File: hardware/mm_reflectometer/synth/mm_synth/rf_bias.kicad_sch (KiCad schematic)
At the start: 28 parts

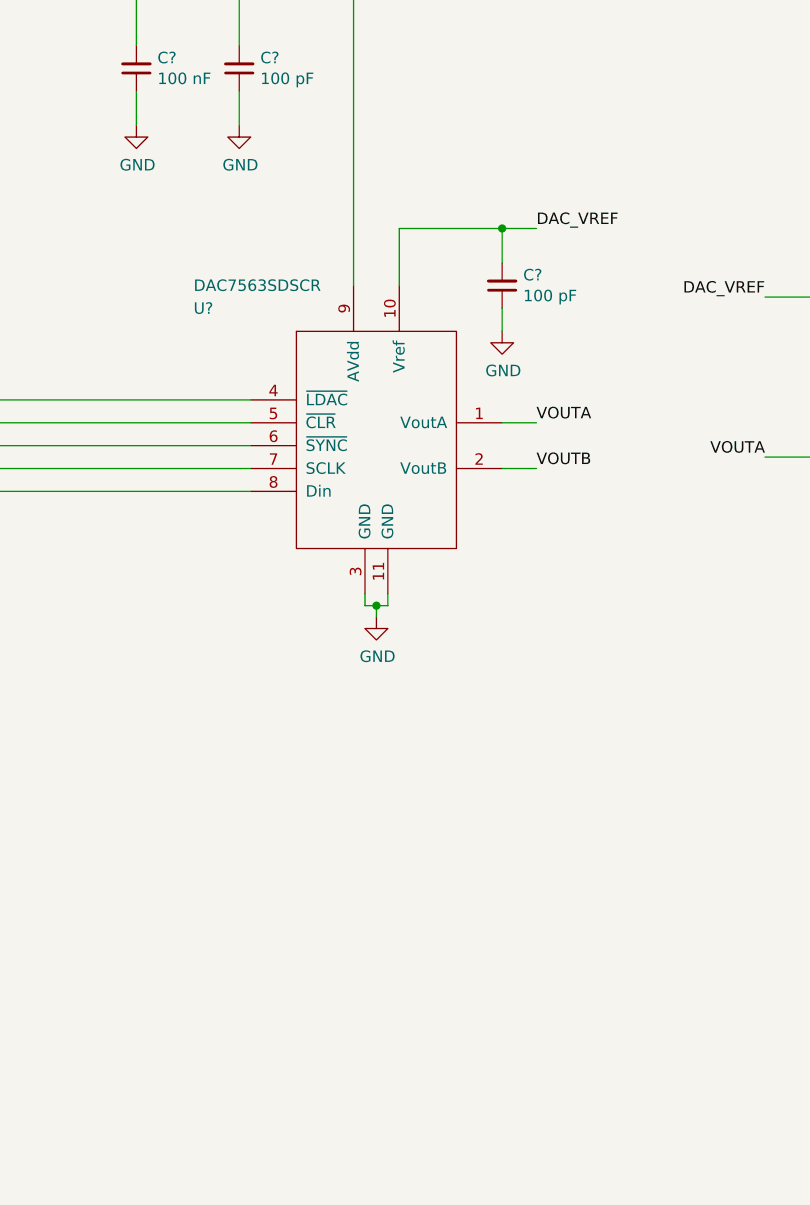
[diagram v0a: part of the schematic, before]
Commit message: adding bias circuitry to mm synth
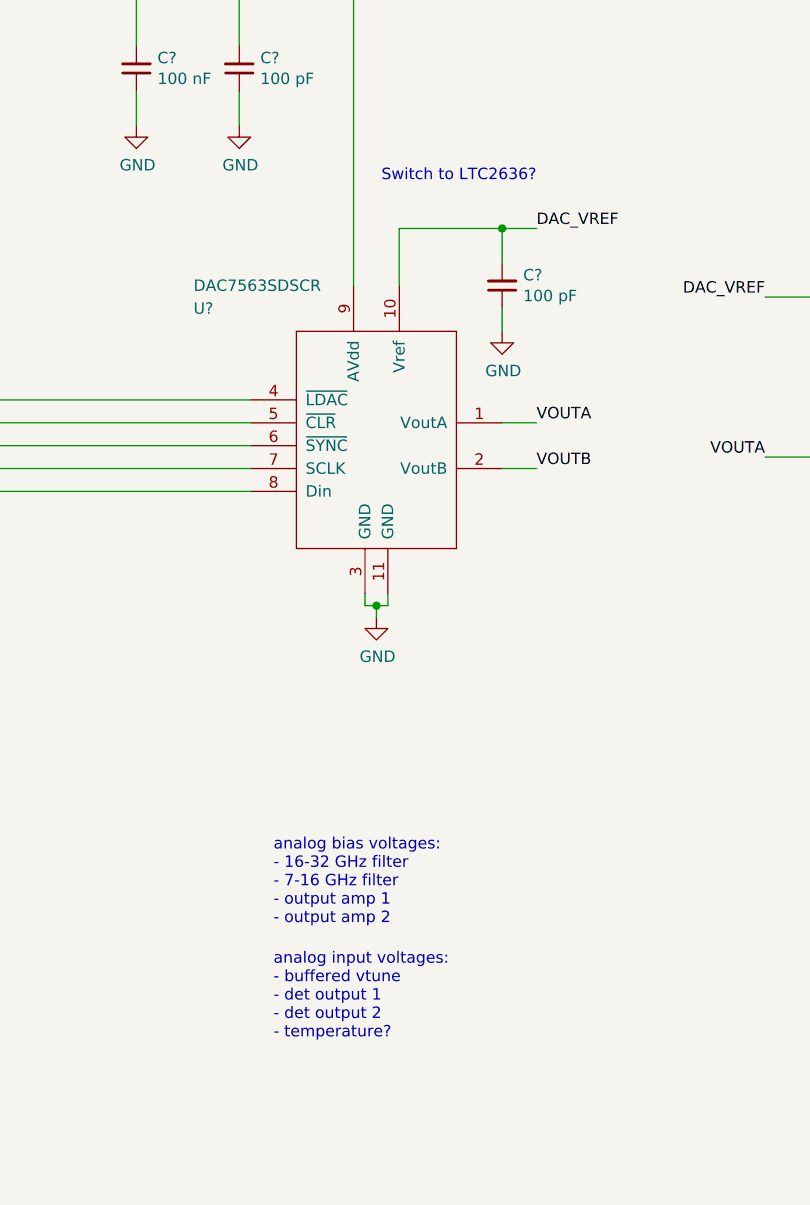
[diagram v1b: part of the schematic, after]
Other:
- note added: "Switch to LTC2636?"
- note added: "analog bias voltages: - 16-32 GHz filter - 7-16 GHz filter - output amp 1 - output amp 2"
- note added: "analog input voltages: - buffered vtune - det output 1 - det output 2 - temperature?"
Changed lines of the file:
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@@
     (stroke (width 0) (type solid) (color 0 0 0 0))
+  )
+  (text "analog bias voltages:\n- 16-32 GHz filter\n- 7-16 GHz filter\n- output amp 1\n- output amp 2"
+    (at 76.2 147.32 0)
+    (effects (font (size 1.27 1.27)) (justify left bottom))
+  )
+  (text "analog input voltages:\n- buffered vtune\n- det output 1\n- det output 2\n- temperature?"
+    (at 76.2 160.02 0)
+    (effects (font (size 1.27 1.27)) (justify left bottom))
+  )
+  (text "Switch to LTC2636?" (at 105.41 64.77 180)
+    (effects (font (size 1.27 1.27)) (justify right bottom))
   )
   (text "OUTPUT: 0V to 15V" (at 148.59 143.51 0)
@@
   (symbol (lib_id "power:+15V") (at 167.64 207.01 0) (unit 1)
     (in_bom yes) (on_board yes)
-    (property "Reference" "#PWR?" (id 0) (at 167.64 210.82 0)
+    (property "Reference" "#PWR0258" (id 0) (at 167.64 210.82 0)
       (effects (font (size 1.27 1.27)) hide)
     )
@@
   (symbol (lib_id "power:-5V") (at 167.64 256.54 180) (unit 1)
     (in_bom yes) (on_board yes)
-    (property "Reference" "#PWR?" (id 0) (at 167.64 259.08 0)
+    (property "Reference" "#PWR0260" (id 0) (at 167.64 259.08 0)
       (effects (font (size 1.27 1.27)) hide)
     )
@@
   (symbol (lib_id "power:GND") (at 27.94 88.9 270) (unit 1)
     (in_bom yes) (on_board yes)
-    (property "Reference" "#PWR?" (id 0) (at 21.59 88.9 0)
+    (property "Reference" "#PWR0257" (id 0) (at 21.59 88.9 0)
       (effects (font (size 1.27 1.27)) hide)
     )
@@
   (symbol (lib_id "power:GND") (at 60.96 58.42 0) (unit 1)
     (in_bom yes) (on_board yes)
-    (property "Reference" "#PWR?" (id 0) (at 60.96 64.77 0)
+    (property "Reference" "#PWR0255" (id 0) (at 60.96 64.77 0)
       (effects (font (size 1.27 1.27)) hide)
     )
@@
   (symbol (lib_id "power:GND") (at 72.39 58.42 0) (unit 1)
     (in_bom yes) (on_board yes)
-    (property "Reference" "#PWR?" (id 0) (at 72.39 64.77 0)
+    (property "Reference" "#PWR0256" (id 0) (at 72.39 64.77 0)
       (effects (font (size 1.27 1.27)) hide)
     )
@@
   (symbol (lib_id "power:GND") (at 87.63 113.03 0) (unit 1)
     (in_bom yes) (on_board yes)
-    (property "Reference" "#PWR?" (id 0) (at 87.63 119.38 0)
+    (property "Reference" "#PWR0254" (id 0) (at 87.63 119.38 0)
       (effects (font (size 1.27 1.27)) hide)
     )
@@
   (symbol (lib_id "power:GND") (at 101.6 81.28 0) (unit 1)
     (in_bom yes) (on_board yes)
-    (property "Reference" "#PWR?" (id 0) (at 101.6 87.63 0)
+    (property "Reference" "#PWR0253" (id 0) (at 101.6 87.63 0)
       (effects (font (size 1.27 1.27)) hide)
     )
@@
   (symbol (lib_id "power:GND") (at 147.32 111.76 0) (unit 1)
     (in_bom yes) (on_board yes)
-    (property "Reference" "#PWR?" (id 0) (at 147.32 118.11 0)
+    (property "Reference" "#PWR0252" (id 0) (at 147.32 118.11 0)
       (effects (font (size 1.27 1.27)) hide)
     )
@@
   (symbol (lib_id "power:GND") (at 165.1 189.23 0) (unit 1)
     (in_bom yes) (on_board yes)
-    (property "Reference" "#PWR?" (id 0) (at 165.1 195.58 0)
+    (property "Reference" "#PWR0259" (id 0) (at 165.1 195.58 0)
       (effects (font (size 1.27 1.27)) hide)
     )
@@
   (symbol (lib_id "power:GND") (at 177.8 217.17 0) (mirror y) (unit 1)
     (in_bom yes) (on_board yes)
-    (property "Reference" "#PWR?" (id 0) (at 177.8 223.52 0)
+    (property "Reference" "#PWR0262" (id 0) (at 177.8 223.52 0)
       (effects (font (size 1.27 1.27)) hide)
     )
@@
   (symbol (lib_id "power:GND") (at 177.8 241.3 0) (mirror x) (unit 1)
     (in_bom yes) (on_board yes)
-    (property "Reference" "#PWR?" (id 0) (at 177.8 234.95 0)
+    (property "Reference" "#PWR0263" (id 0) (at 177.8 234.95 0)
       (effects (font (size 1.27 1.27)) hide)
     )
@@
   (symbol (lib_id "power:GND") (at 189.23 217.17 0) (mirror y) (unit 1)
     (in_bom yes) (on_board yes)
-    (property "Reference" "#PWR?" (id 0) (at 189.23 223.52 0)
+    (property "Reference" "#PWR0261" (id 0) (at 189.23 223.52 0)
       (effects (font (size 1.27 1.27)) hide)
     )
@@
   (symbol (lib_id "power:GND") (at 189.23 241.3 0) (mirror x) (unit 1)
     (in_bom yes) (on_board yes)
-    (property "Reference" "#PWR?" (id 0) (at 189.23 234.95 0)
+    (property "Reference" "#PWR0264" (id 0) (at 189.23 234.95 0)
       (effects (font (size 1.27 1.27)) hide)
     )
@@
   (symbol (lib_id "power:GND") (at 223.52 73.66 0) (unit 1)
     (in_bom yes) (on_board yes)
-    (property "Reference" "#PWR?" (id 0) (at 223.52 80.01 0)
+    (property "Reference" "#PWR0266" (id 0) (at 223.52 80.01 0)
       (effects (font (size 1.27 1.27)) hide)
     )
@@
   (symbol (lib_id "power:GND") (at 241.3 74.93 0) (unit 1)
     (in_bom yes) (on_board yes)
-    (property "Reference" "#PWR?" (id 0) (at 241.3 81.28 0)
+    (property "Reference" "#PWR0267" (id 0) (at 241.3 81.28 0)
       (effects (font (size 1.27 1.27)) hide)
     )
@@
   (symbol (lib_id "power:GND") (at 251.46 33.02 0) (mirror y) (unit 1)
     (in_bom yes) (on_board yes)
-    (property "Reference" "#PWR?" (id 0) (at 251.46 39.37 0)
+    (property "Reference" "#PWR0265" (id 0) (at 251.46 39.37 0)
       (effects (font (size 1.27 1.27)) hide)
     )
@@
   (symbol (lib_id "power:GND") (at 262.89 33.02 0) (mirror y) (unit 1)
     (in_bom yes) (on_board yes)
-    (property "Reference" "#PWR?" (id 0) (at 262.89 39.37 0)
-      (effects (font (size 1.27 1.27)) hide)
-    )
+    (property "Reference" "#PWR0268" (id 0) (at 262.89 39.37 0)
+      (effects (font (size 1.27 1.27)) hide)
+    )

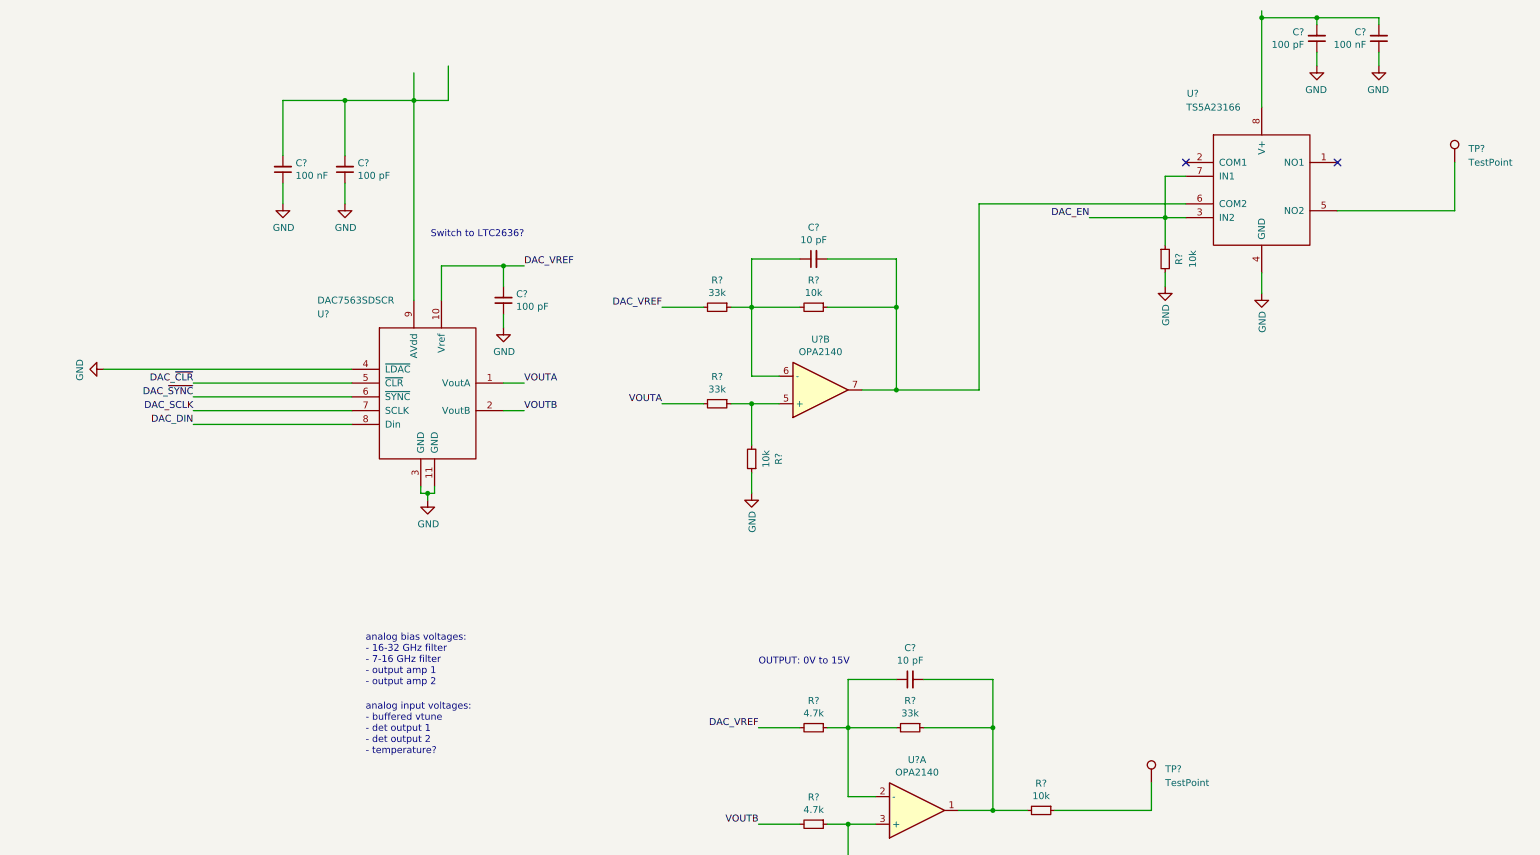
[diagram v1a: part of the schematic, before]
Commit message: added dac to mm_synth for vtune/adjstable bias, added ADC for telemetry
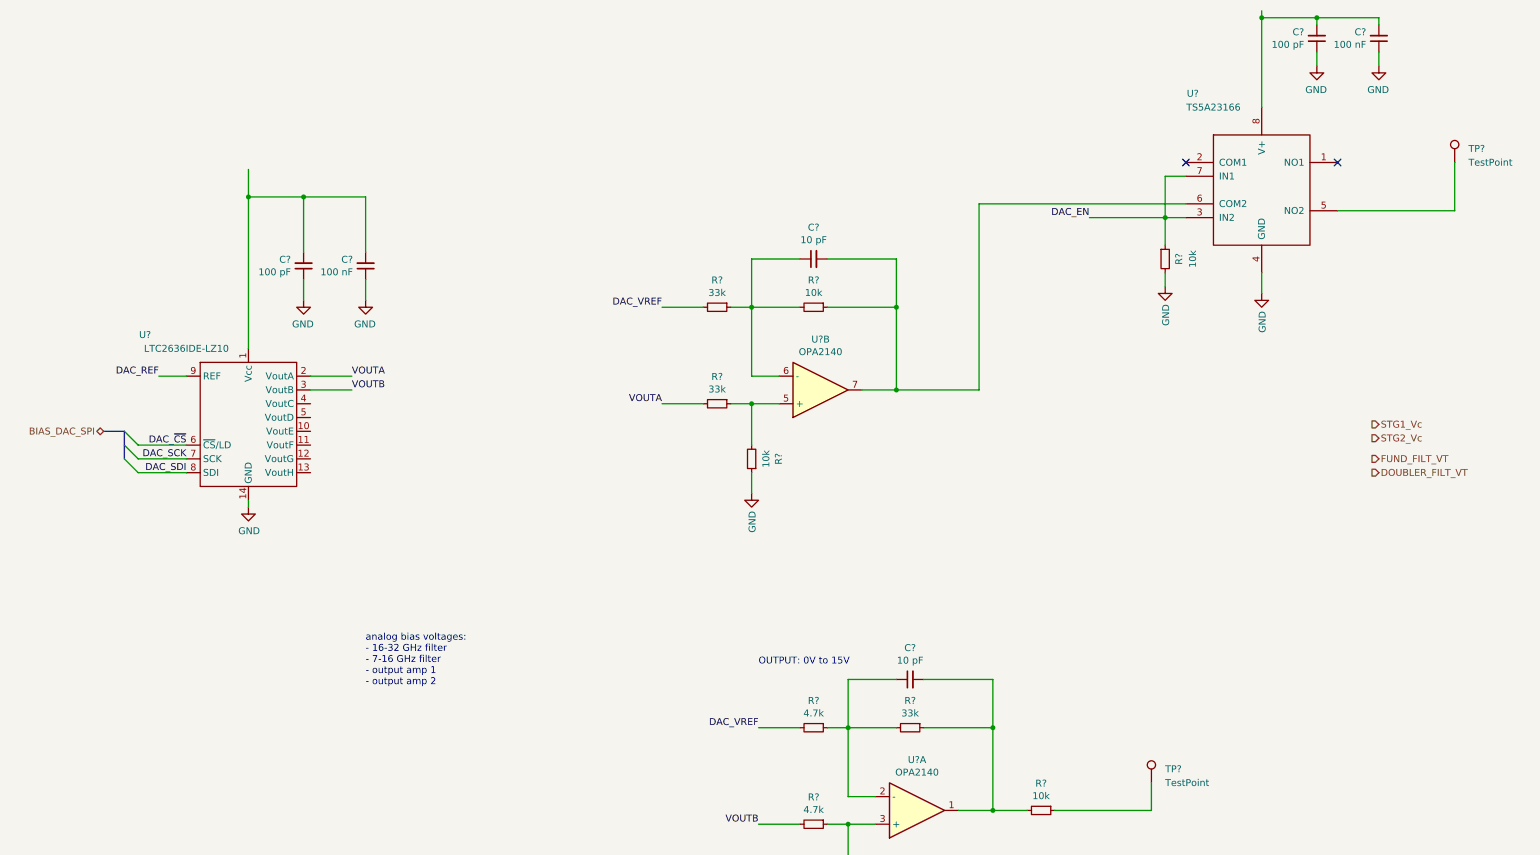
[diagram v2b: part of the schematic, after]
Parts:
- removed C?: 100 pF, Capacitor_SMD:C_0402_1005Metric, symbol Device:C_Small
- removed U?: DAC7563SDSCR, Housings_DFN_QFN:DFN-10-1EP_3x3mm_Pitch0.5mm, symbol vna_mm:DAC7563SDSCR
- added U?: LTC2636IDE-LZ10, Package_DFN_QFN:DFN-14-1EP_3x4mm_P0.5mm_EP1.7x3.3mm, symbol jtk_rf:LTC2636IDE-LZ10
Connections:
- net GND: now also U?.14 (GND), U?.15 (EP)
- net VOUTA: now also U?.2 (VoutA)
- net VOUTB: now also U?.3 (VoutB)
- net at C?.2, C?.2: now also U?.1 (Vcc)
- new net DAC_REF: U?.9 (REF)
- new net DAC_SCK: U?.7 (SCK)
- new net DAC_SDI: U?.8 (SDI)
- new net DAC_~CS: U?.6 (~CS~/LD)
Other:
- note removed: "Switch to LTC2636?"
- note removed: "analog input voltages: - buffered vtune - det output 1 - det output 2 - temperature?"
- moved on the sheet: C?

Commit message: schematic work on mm synth -- starting voltage regulation
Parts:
- removed TP? (x2): TestPoint, TestPoint:TestPoint_Keystone_5015_Micro-Minature, symbol Connector:TestPoint
- removed U? (x2): OPA2140, Package_SO:MSOP-8_3x3mm_P0.65mm, symbol vna_mm_synth-rescue:Opamp_Dual_Generic-Device
- added C? (x6): 100 nF, Capacitor_SMD:C_0402_1005Metric, symbol Device:C_Small
- added C? (x6): 100 pF, Capacitor_SMD:C_0402_1005Metric, symbol Device:C_Small
- added C?: 4.7 uF, Capacitor_SMD:C_0402_1005Metric, symbol Device:C_Small
- added C? (x2): 10 pF, Capacitor_SMD:C_0402_1005Metric, symbol Device:C_Small
- added FB?: BLM18BB471SN1D, symbol Device:FerriteBead_Small
- added R? (x4): 33k, Resistor_SMD:R_0402_1005Metric, symbol Device:R_Small
- added R? (x4): 10k, Resistor_SMD:R_0402_1005Metric, symbol Device:R_Small
- added R?: 4.7k, Resistor_SMD:R_0402_1005Metric, symbol Device:R_Small
- added U? (x4): TLV9151IDCKR, Package_TO_SOT_SMD:SOT-353_SC-70-5, symbol Amplifier_Operational:TLV9001IDCK
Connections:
- net -5V is gone; now on net GND: C?.2, C?.2, U?.4 (V-)
- net DAC_VREF is gone; now on net DAC_REF_2P5V: R?.2, R?.2
- net +15V: now also C?.2, C?.2, C?.2, C?.2, U?.5 (V+), U?.5 (V+)
- net DOUBLER_FILT_VT: now also R?.1
- net FUND_FILT_VT: now also R?.1
- net GND: now also C?.1, C?.1, C?.1, C?.1, C?.1, C?.1, C?.1, C?.1, C?.1, C?.1, C?.1, C?.1, C?.1, R?.1, R?.1, U?.2 (V-), U?.2 (V-)
- net STG1_Vc: now also U?.1 (NO1)
- net STG2_Vc: now also U?.5 (NO2)
- net VOUTA: now also R?.2, R?.2
- net +5VA: now reaches C?.2, C?.2, U?.8 (V+)
- net +5VA: now also C?.2, C?.2, C?.2, C?.2, FB?.1, U?.5 (V+), U?.5 (V+)
- net at C?.2, R?.1, U?.6 (COM2): now also U?.4
- net at C?.1, R?.1, R?.2: now also U?.3 (-) (x2)
- net at C?.2, R?.1, R?.2: now also U?.4
- net at R?.1, R?.2: now also U?.1 (+) (x2)
- net at U?.2 (COM1): now also C?.2, R?.1, U?.4
- net at C?.2, C?.2, U?.1 (Vcc): now also C?.2, FB?.2
- net VOUTC: now reaches U?.4 (VoutC)
- net VOUTD: now reaches U?.5 (VoutD)
- net DAC_EN renamed AMP_Vc_EN
- net DAC_REF renamed DAC_REF_2P5V
- net DAC_REF_2P5V: now also R?.2, R?.2
- new net: R?.1, R?.2, U?.1 (+) (x2)
- new net: C?.1, R?.1, R?.2, U?.3 (-) (x2)
- new net: C?.2, R?.1, R?.2, U?.4
- new net -5VA: C?.2, C?.2, C?.2, C?.2, U?.2 (V-), U?.2 (V-)
- no-connect marks 2 -> 0
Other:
- note added: "-0.9V to 1.1V"
- note added: "0-15V"
- note added: "2.7V to 5.5V supply"
- note added: "Replace op-ampps with TLV9152?"
- note added: "TODO: CHECK OP AMP CIRCUIT VALUES"
- note added: "TODO: REPLACE WITH SWITCH THAT CAN HANDLE POSTIIVE AND NEGATIVE VOLTAGES"
- moved on the sheet: C?, R?, U?, U?C

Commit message: library updates
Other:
- note added: "Use TMUX6136?"
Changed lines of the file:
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@@
     (effects (font (size 1.27 1.27)) (justify right bottom))
+  )
+  (text "Use TMUX6136?" (at 332.74 76.835 180)
+    (effects (font (size 3 3) (thickness 0.6) bold) (justify right bottom))
   )
   (text "-0.9V to 1.1V" (at 346.71 113.03 180)

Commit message: adding digital connections to synth schematic
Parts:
- removed U?: TS5A23166, v:VSSOP-8, symbol vna_mm:TS5A23166
- added C?: 100 nF, Capacitor_SMD:C_0402_1005Metric, symbol Device:C_Small
- added R? (x2): 10k, Resistor_SMD:R_0402_1005Metric, symbol Device:R_Small
- added TP? (x4): TestPoint, symbol Connector:TestPoint
- added U?: TMUX6136, Package_SO:TSSOP-14_4.4x5mm_P0.65mm, symbol jtk_rf:TMUX6136
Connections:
- net +5VA: now also U?.13 (Vdd)
- net -5VA: now also C?.2, U?.5 (Vss)
- net AMP_Vc_EN: now also U?.1 (SEL1), U?.9 (SEL2)
- net GND: now also C?.1, U?.14 (NC), U?.15 (NC), U?.16 (NC), U?.6 (GND), U?.7 (NC), U?.8 (NC)
- net STG1_Vc: now also U?.3 (D1)
- net STG2_Vc: now also U?.11 (D2)
- net at C?.2, R?.1, U?.4: now also R?.2 (x2)
- net at U?.10 (VoutE): now also TP?.1
- net at U?.11 (VoutF): now also TP?.1
- new net: TP?.1, U?.10 (S2A)
- new net: R?.1, U?.12 (S2B)
- new net: TP?.1, U?.2 (S1A)
- new net: R?.1, U?.4 (S1B)
- no-connect marks 0 -> 2
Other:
- note added: "3.3V CMOS"
- note added: "SELx A B 0 OFF ON 1 ON OFF"
- note removed: "TODO: REPLACE WITH SWITCH THAT CAN HANDLE POSTIIVE AND NEGATIVE VOLTAGES"
- note removed: "Use TMUX6136?"
- moved on the sheet: C?, R?
